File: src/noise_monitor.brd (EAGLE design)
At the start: 53 x 48 mm, 72 parts, among them IC2 MCP73831/OT, T1 S8050, T2 S8050, U2 TEXAS_INSTRUMENTS_SN74HC125TE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, U4 ESP8266-12E/ESP-12E, U5 CP2102N-A02-GQFN28, U6 LP2989AILD-3.3, X2 SIMLOCK-C707_10M006_512_2

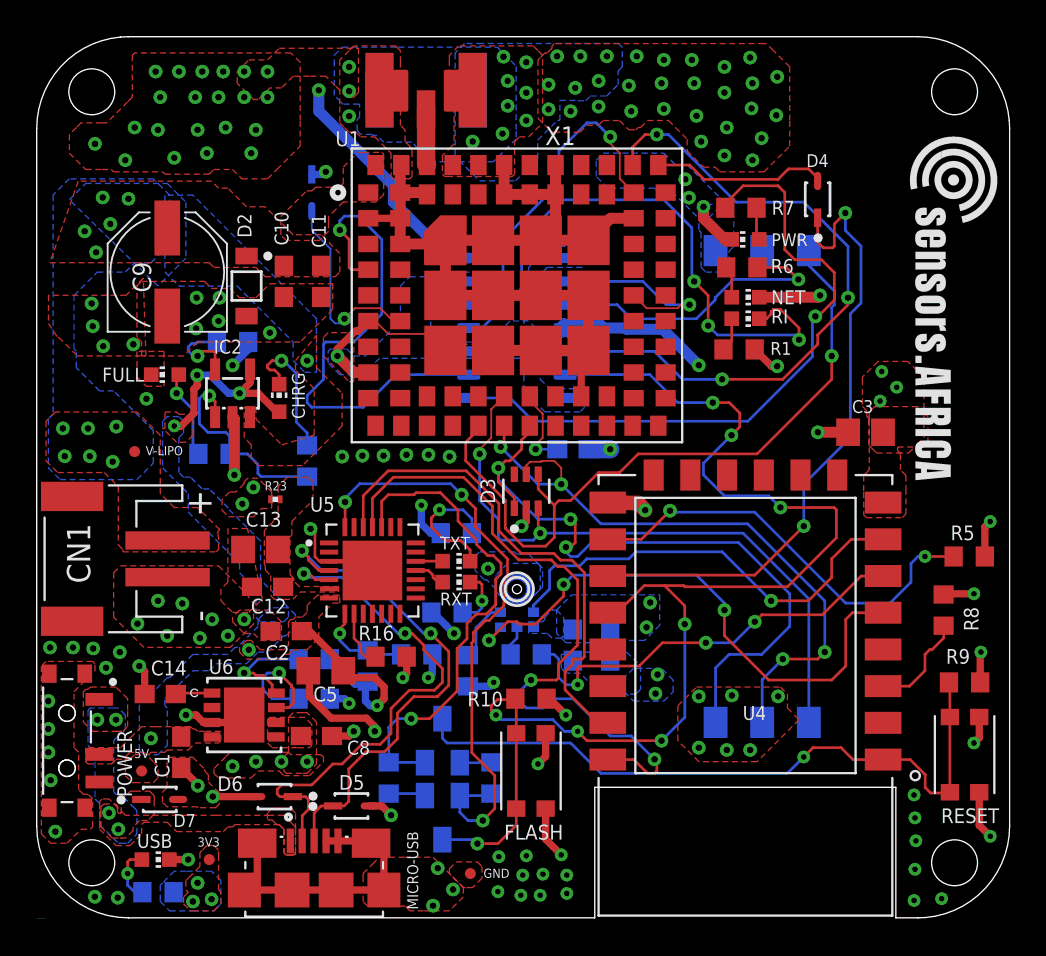
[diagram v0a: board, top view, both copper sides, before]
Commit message: adjusted mounting hole diameter
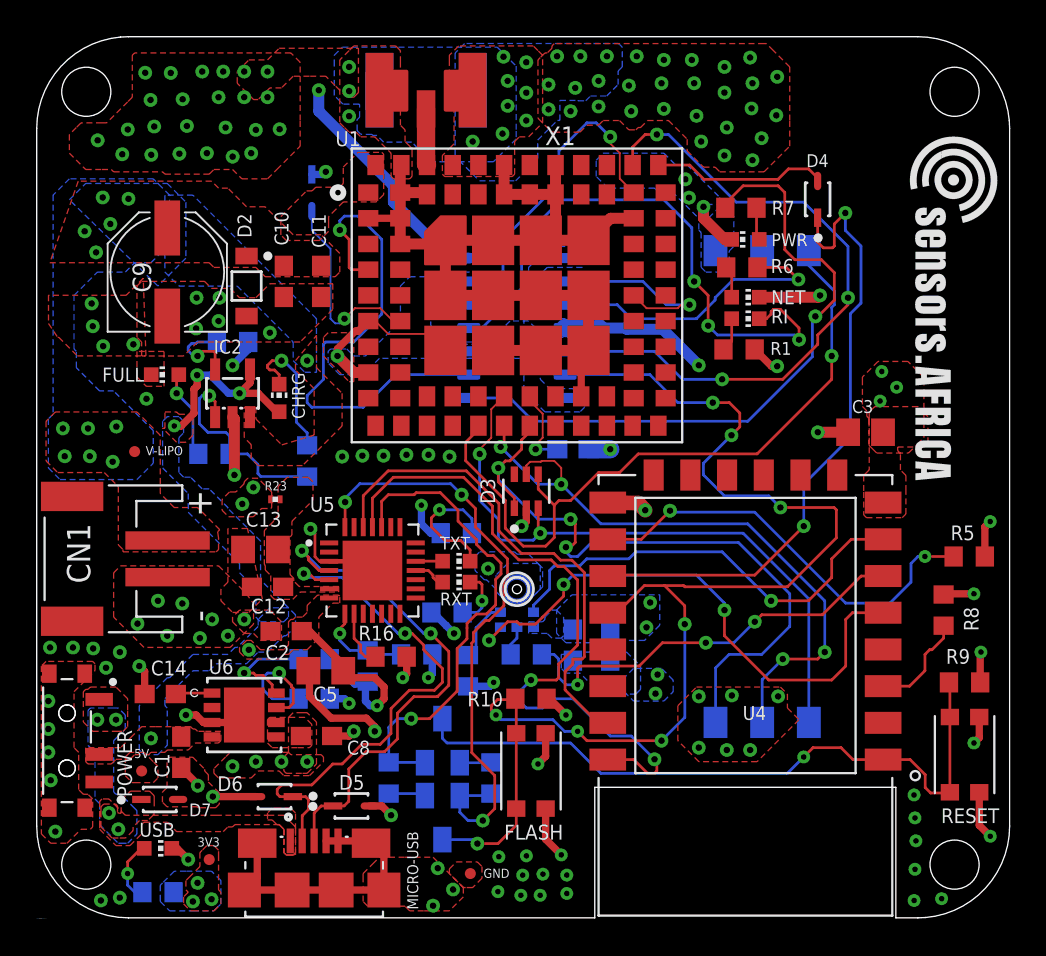
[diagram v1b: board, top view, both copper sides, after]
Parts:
- moved USB 0.62 mm to (6.61, 3.79)
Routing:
- net GND: track 139.8 -> 139.9 mm, vias 154 -> 157
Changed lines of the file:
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@@
 <drawing>
 <settings>
-<setting alwaysvectorfont="no"/>
+<setting alwaysvectorfont="yes"/>
 <setting verticaltext="up"/>
 </settings>
@@
 <circle x="26.162" y="17.907" radius="0.647575" width="0.1524" layer="25"/>
 <circle x="26.162" y="17.907" radius="0.898025" width="0.1524" layer="25"/>
-<hole x="3" y="3" drill="2.5"/>
-<hole x="50" y="3" drill="2.5"/>
-<hole x="50" y="45" drill="2.5"/>
-<hole x="3" y="45" drill="2.5"/>
 <wire x1="1.4005" y1="8.527" x2="1.2465" y2="8.3515" width="0" layer="20" curve="30.0001"/>
 <wire x1="1.4005" y1="8.527" x2="1.4515" y2="8.5565" width="0" layer="20"/>
@@
 <rectangle x1="52.29" y1="40.17" x2="52.37" y2="40.18" layer="21" rot="R270"/>
 <text x="0" y="-0.05" size="0.02" layer="21" font="vector">/Users/mcleans/Desktop/Logo-Files-01.bmp</text>
+<hole x="2.7" y="45" drill="2.675"/>
+<hole x="2.7" y="2.9" drill="2.675"/>
+<hole x="50" y="45" drill="2.675"/>
+<hole x="50" y="2.9" drill="2.675"/>
 </plain>
 <attributes>
@@
 <attribute name="VALUE" x="47.620109375" y="2.5012" size="1.27118125" layer="27" rot="R180"/>
 </element>
-<element name="USB" library="led" library_urn="urn:adsk.eagle:library:259" package="CHIP-LED0603" package3d_urn="urn:adsk.eagle:package:15819/3" value="" x="6.477" y="3.175" smashed="yes" rot="R270">
-<attribute name="NAME" x="5.461" y="3.81" size="0.762" layer="25"/>
-<attribute name="POPULARITY" value="26" x="-76.073" y="-59.055" size="1.778" layer="27" rot="R270" display="off"/>
-<attribute name="VALUE" x="5.842" y="1.27" size="1.27" layer="27"/>
+<element name="USB" library="led" library_urn="urn:adsk.eagle:library:259" package="CHIP-LED0603" package3d_urn="urn:adsk.eagle:package:15819/3" value="" x="6.607" y="3.785" smashed="yes" rot="R270">
+<attribute name="NAME" x="5.591" y="4.42" size="0.762" layer="25"/>
+<attribute name="POPULARITY" value="26" x="-75.943" y="-58.445" size="1.778" layer="27" rot="R270" display="off"/>
+<attribute name="VALUE" x="5.972" y="1.88" size="1.27" layer="27"/>
 </element>
 <element name="X2" library="noise_monitor" library_urn="urn:adsk.eagle:library:35677466" package="C707_10M006_512_2" package3d_urn="urn:adsk.eagle:package:35677574/2" value="SIMLOCK-C707_10M006_512_2" x="40.894" y="23.495" smashed="yes" rot="MR90">
@@
 <attribute name="MOUSER_PART_NUMBER" value="512-1N4148WS" x="6.7" y="6.45" size="1.778" layer="27" display="off"/>
 <attribute name="MPN" value="1N4148WS" x="6.7" y="6.45" size="1.778" layer="27" display="off"/>
-<attribute name="NAME" x="7.45" y="4.95" size="0.7" layer="25"/>
+<attribute name="NAME" x="8.3" y="5.53" size="0.7" layer="25"/>
 <attribute name="PACKAGE" value="SOD-323FL" x="6.7" y="6.45" size="1.778" layer="27" display="off"/>
 <attribute name="PREFIX" value="D" x="6.7" y="6.45" size="1.778" layer="27" display="off"/>
@@
 <via x="6.604" y="17.272" extent="1-16" drill="0.35"/>
 <via x="7.112" y="15.367" extent="1-16" drill="0.35"/>
-<via x="6.477" y="46.101" extent="1-16" drill="0.35"/>
 <via x="25.427" y="46.909" extent="1-16" drill="0.35"/>
 <via x="26.67" y="46.609" extent="1-16" drill="0.35"/>
@@
 <via x="17.018" y="45.039" extent="1-16" drill="0.35"/>
 <via x="17.018" y="43.669" extent="1-16" drill="0.35"/>
-<via x="7.747" y="46.101" extent="1-16" drill="0.35"/>
 <via x="9.017" y="46.101" extent="1-16" drill="0.35"/>
 <via x="10.16" y="46.101" extent="1-16" drill="0.35"/>
@@
 <via x="11.303" y="44.704" extent="1-16" drill="0.35"/>
 <via x="9.906" y="44.704" extent="1-16" drill="0.35"/>
-<via x="8.636" y="44.704" extent="1-16" drill="0.35"/>
-<via x="6.731" y="44.704" extent="1-16" drill="0.35"/>
-<via x="6.604" y="42.926" extent="1-16" drill="0.35"/>
-<via x="8.763" y="42.926" extent="1-16" drill="0.35"/>
+<via x="10.673" y="41.466" extent="1-16" drill="0.35"/>
 <via x="10.287" y="43.053" extent="1-16" drill="0.35"/>
 <via x="11.938" y="42.926" extent="1-16" drill="0.35"/>
 <via x="11.684" y="41.656" extent="1-16" drill="0.35"/>
 <via x="9.271" y="41.656" extent="1-16" drill="0.35"/>
-<via x="7.493" y="41.402" extent="1-16" drill="0.35"/>
-<via x="4.826" y="41.275" extent="1-16" drill="0.35"/>
-<via x="5.334" y="43.053" extent="1-16" drill="0.35"/>
-<via x="3.175" y="42.164" extent="1-16" drill="0.35"/>
+<via x="13.233" y="42.962" extent="1-16" drill="0.35"/>
 <via x="28.348" y="46.936" extent="1-16" drill="0.35"/>
 <via x="29.618" y="46.936" extent="1-16" drill="0.35"/>
@@
 <via x="5.588" y="13.716" extent="1-16" drill="0.35"/>
 <via x="8.774" y="7.2" extent="1-16" drill="0.35"/>
-<wire x1="7.227" y1="3.175" x2="8.255" y2="3.175" width="0.4" layer="1"/>
+<wire x1="7.357" y1="3.785" x2="7.645" y2="3.785" width="0.4" layer="1"/>
+<wire x1="7.645" y1="3.785" x2="8.255" y2="3.175" width="0.4" layer="1"/>
 <wire x1="11.954" y1="6.604" x2="9.594" y2="6.604" width="0.4" layer="1"/>
 <via x="8.255" y="3.175" extent="1-16" drill="0.35"/>
@@
 <via x="47.793" y="0.945" extent="1-16" drill="0.3"/>
 <via x="49.293" y="1.045" extent="1-16" drill="0.3"/>
-<via x="4.416" y="1.099" extent="1-16" drill="0.35"/>
-<via x="3.166" y="1.149" extent="1-16" drill="0.35"/>
+<via x="4.526" y="1.099" extent="1-16" drill="0.35"/>
+<via x="3.496" y="0.949" extent="1-16" drill="0.35"/>
 <via x="16.641" y="25.126" extent="1-16" drill="0.35"/>
 <via x="17.741" y="25.176" extent="1-16" drill="0.35"/>
@@
 <wire x1="9.5504" y1="10.6426" x2="10.8966" y2="10.6426" width="0.4" layer="1"/>
 <wire x1="10.8966" y1="10.6426" x2="11.303" y2="11.049" width="0.4" layer="1"/>
+<via x="7.771" y="41.626" extent="1-16" drill="0.35"/>
+<via x="4.661" y="41.596" extent="1-16" drill="0.35"/>
+<via x="3.321" y="42.356" extent="1-16" drill="0.35"/>
+<via x="4.961" y="42.946" extent="1-16" drill="0.35"/>
+<via x="6.241" y="41.566" extent="1-16" drill="0.35"/>
+<via x="6.401" y="43.106" extent="1-16" drill="0.35"/>
+<via x="8.181" y="43.136" extent="1-16" drill="0.35"/>
+<via x="7.951" y="44.596" extent="1-16" drill="0.35"/>
+<via x="7.301" y="46.026" extent="1-16" drill="0.35"/>
+<via x="5.911" y="46.036" extent="1-16" drill="0.35"/>
+<via x="6.201" y="44.556" extent="1-16" drill="0.35"/>
 </signal>
 <signal name="+5V" class="1">
@@
 <via x="4.953" y="2.413" extent="1-16" drill="0.3"/>
 <wire x1="5.671" y1="1.314" x2="5.754" y2="1.397" width="0.15" layer="16"/>
-<wire x1="5.08" y1="3.175" x2="4.953" y2="3.048" width="0.15" layer="1"/>
+<wire x1="5.69" y1="3.785" x2="4.953" y2="3.048" width="0.15" layer="1"/>
 <wire x1="4.953" y1="3.048" x2="4.953" y2="2.413" width="0.15" layer="1"/>
-<wire x1="5.727" y1="3.175" x2="5.08" y2="3.175" width="0.15" layer="1"/>
+<wire x1="5.857" y1="3.785" x2="5.69" y2="3.785" width="0.15" layer="1"/>
 <wire x1="4.953" y1="2.413" x2="4.953" y2="1.778" width="0.15" layer="16"/>
 <wire x1="4.953" y1="1.778" x2="5.417" y2="1.314" width="0.15" layer="16"/>
